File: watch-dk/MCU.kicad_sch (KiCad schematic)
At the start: 40 parts, among them IC301 FAN5624UMPX, IC302 MX25U51245GZ4I00, IC303 USBLC6-2P6, IC304 NTS0104GU12, J301 Jumper, J302 Jumper, J303 Jumper, J304 Jumper, M301 NORA-B106, X301 Power, X302 Power, X303 Device, X304 GPIO, X305 UART, X306 IO Power, X307 Display, X308 Touch Power, X309 LED Power, X310 DEBUG

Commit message: Task: Issue #129
Signed-off-by: Daniel Kampert <DanielKampert@kampis-elektroecke.de>
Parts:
- X301, X302: value Power -> Current
- X306: value IO Power -> IO Current
- X308: value Touch Power -> Touch Current
- X309: value LED Power -> LED Current
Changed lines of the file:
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@@
 			)
 		)
-		(property "Value" "Power"
+		(property "Value" "Current"
 			(at 54.61 63.5 0)
 			(effects
@@
 			)
 		)
-		(property "Value" "Power"
+		(property "Value" "Current"
 			(at 261.62 186.69 0)
 			(effects
@@
 			)
 		)
-		(property "Value" "Touch Power"
+		(property "Value" "Touch Current"
 			(at 365.76 118.1099 0)
 			(effects
@@
 			)
 		)
-		(property "Value" "IO Power"
+		(property "Value" "IO Current"
 			(at 341.63 118.1099 0)
 			(effects
@@
 			)
 		)
-		(property "Value" "LED Power"
+		(property "Value" "LED Current"
 			(at 377.19 166.3699 90)
 			(effects

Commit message: Feature: Issue #131
- Fix wrong page numbers
- Update reference designators to match the page numbers

Signed-off-by: Daniel Kampert <DanielKampert@kampis-elektroecke.de>
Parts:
- added S601: RESET, Wuerth:WS-TASV-6x6, symbol Switch:SW_Push
- renumbered C301 to C601, C302 to C602, C303 to C603, C304 to C604, IC301 to IC601, IC303 to IC602, IC302 to IC603, IC304 to IC604, J301 to J601, J302 to J602, J303 to J603, J304 to J604, M301 to M601, R301 to R601, R303 to R602, R304 to R603, R305 to R604, R306 to R605, R307 to R606, R308 to R607, R309 to R608, R310 to R609, R311 to R610, R312 to R611, R302 to R612, R315 to R613, R316 to R614, R313 to R615, R314 to R616, TP301 to TP601, X310 to X601, X301 to X602, X303 to X603, X305 to X604, X304 to X605, X302 to X606, X306 to X607, X307 to X608, X308 to X609, X309 to X610
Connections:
- net GND: now also S601.2
- net RESETn: now also S601.1
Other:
- moved on the sheet: C602, IC603, J601, R612, X606

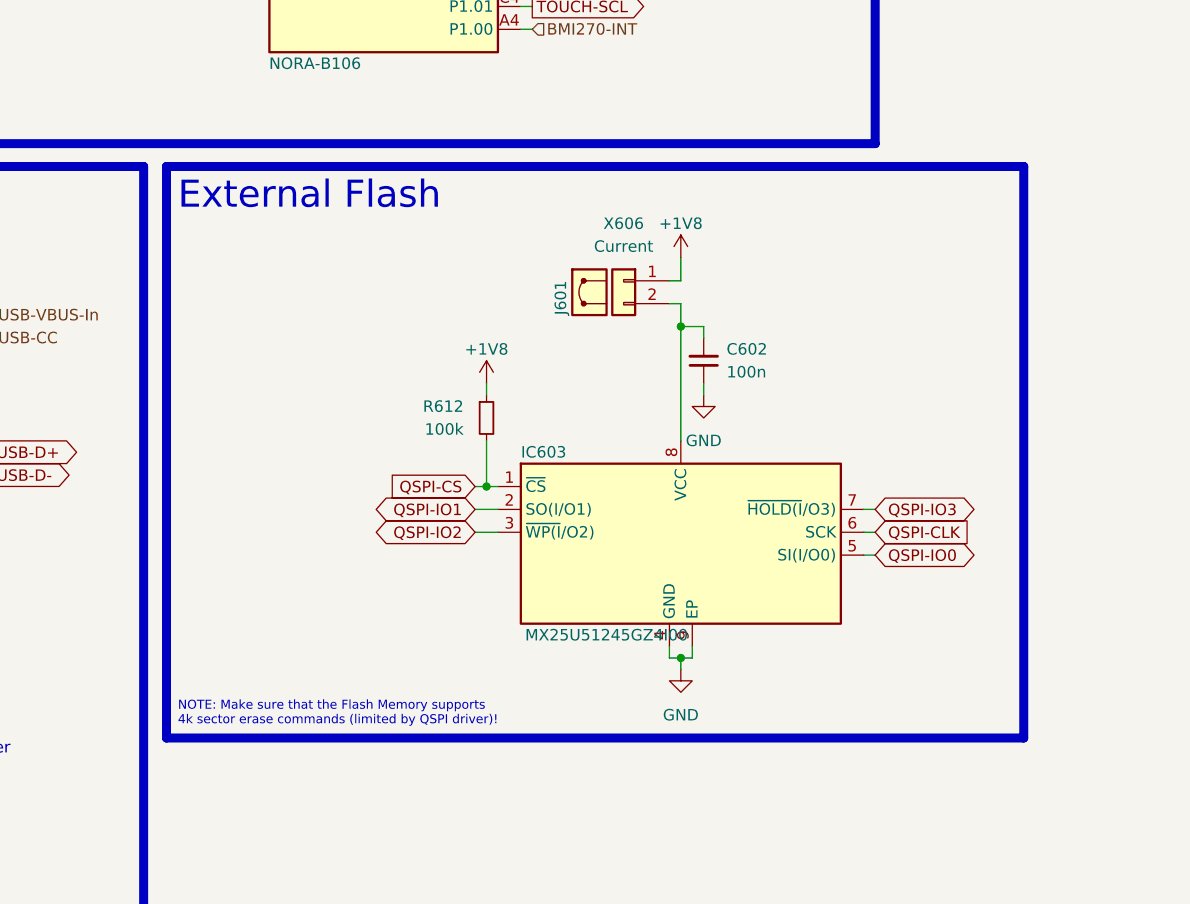
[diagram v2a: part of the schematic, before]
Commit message: Bug: Issue #132
Signed-off-by: Daniel Kampert <DanielKampert@kampis-elektroecke.de>
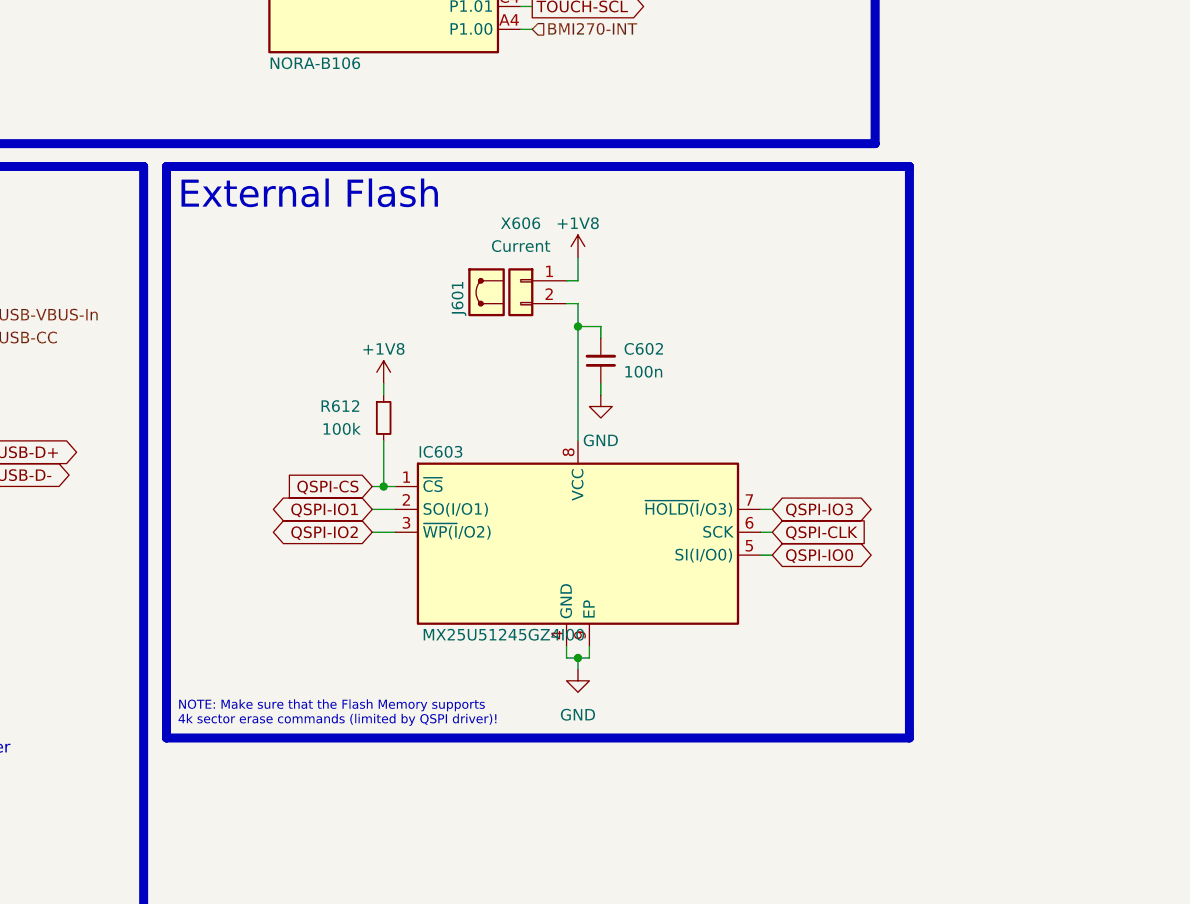
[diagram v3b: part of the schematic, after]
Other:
- moved on the sheet: C602, IC603, J601, R612, X606

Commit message: Feature: Issue #133
Signed-off-by: Daniel Kampert <DanielKampert@kampis-elektroecke.de>
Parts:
- IC604: symbol NXP:NTS0104GU12 -> NXP:NTS0104GU12 (XQFN12)
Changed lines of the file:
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@@
 	)
 	(symbol
-		(lib_id "NXP:NTS0104GU12")
+		(lib_id "NXP:NTS0104GU12 (XQFN12)")
 		(at 351.79 76.2 0)
 		(unit 1)
@@
 		)
 		(property "Footprint" "Package_QFN:XQFN-12-1.7x2mm_P0.4mm"
-			(at 353.06 73.66 0)
+			(at 351.79 76.2 0)
 			(effects
 				(font
@@
 		)
 		(property "Datasheet" "https://www.nxp.com/docs/en/data-sheet/NTS0104.pdf"
-			(at 353.06 73.66 0)
+			(at 351.79 76.2 0)
 			(effects
 				(font

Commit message: Bug: Issue #134
Signed-off-by: Daniel Kampert <DanielKampert@kampis-elektroecke.de>
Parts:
- C601: manf# 04023D105KAT2A -> 0402YC105JAT2A; mouser# 581-04023D105KAT2A -> 581-0402YC105JAT2A
- IC601: value FAN5624UMPX -> FAN5622SX; footprint Package_DFN_QFN:UQFN-10_1.4x1.8mm_P0.4mm -> Package_TO_SOT_SMD:TSOT-23-6; symbol ON Semiconductor:FAN5624 -> ON Semiconductor:FAN5622SX; manf# FAN5624UMPX -> FAN5622SX; mouser# 512-FAN5624UMPX -> 512-FAN5622SX
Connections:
- net DISPLAY-BLK: now also IC601.1 (CTRL); no longer IC601.7 (CTRL)
- net GND: now also IC601.2 (GND), R601.1; no longer IC601.6 (GND), R601.2
- net LEDK1: now also IC601.6 (LED1); no longer IC601.8 (LED1)
- net LEDK2: now also IC601.4 (LED2); no longer IC601.10 (LED2)
- net at IC601.3 (VIN): now also C601.2, R602.2; no longer R601.1
- new net: IC601.5 (ISET), R601.2
- no-connect marks 13 -> 11
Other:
- moved on the sheet: C601, J602, J604, R601

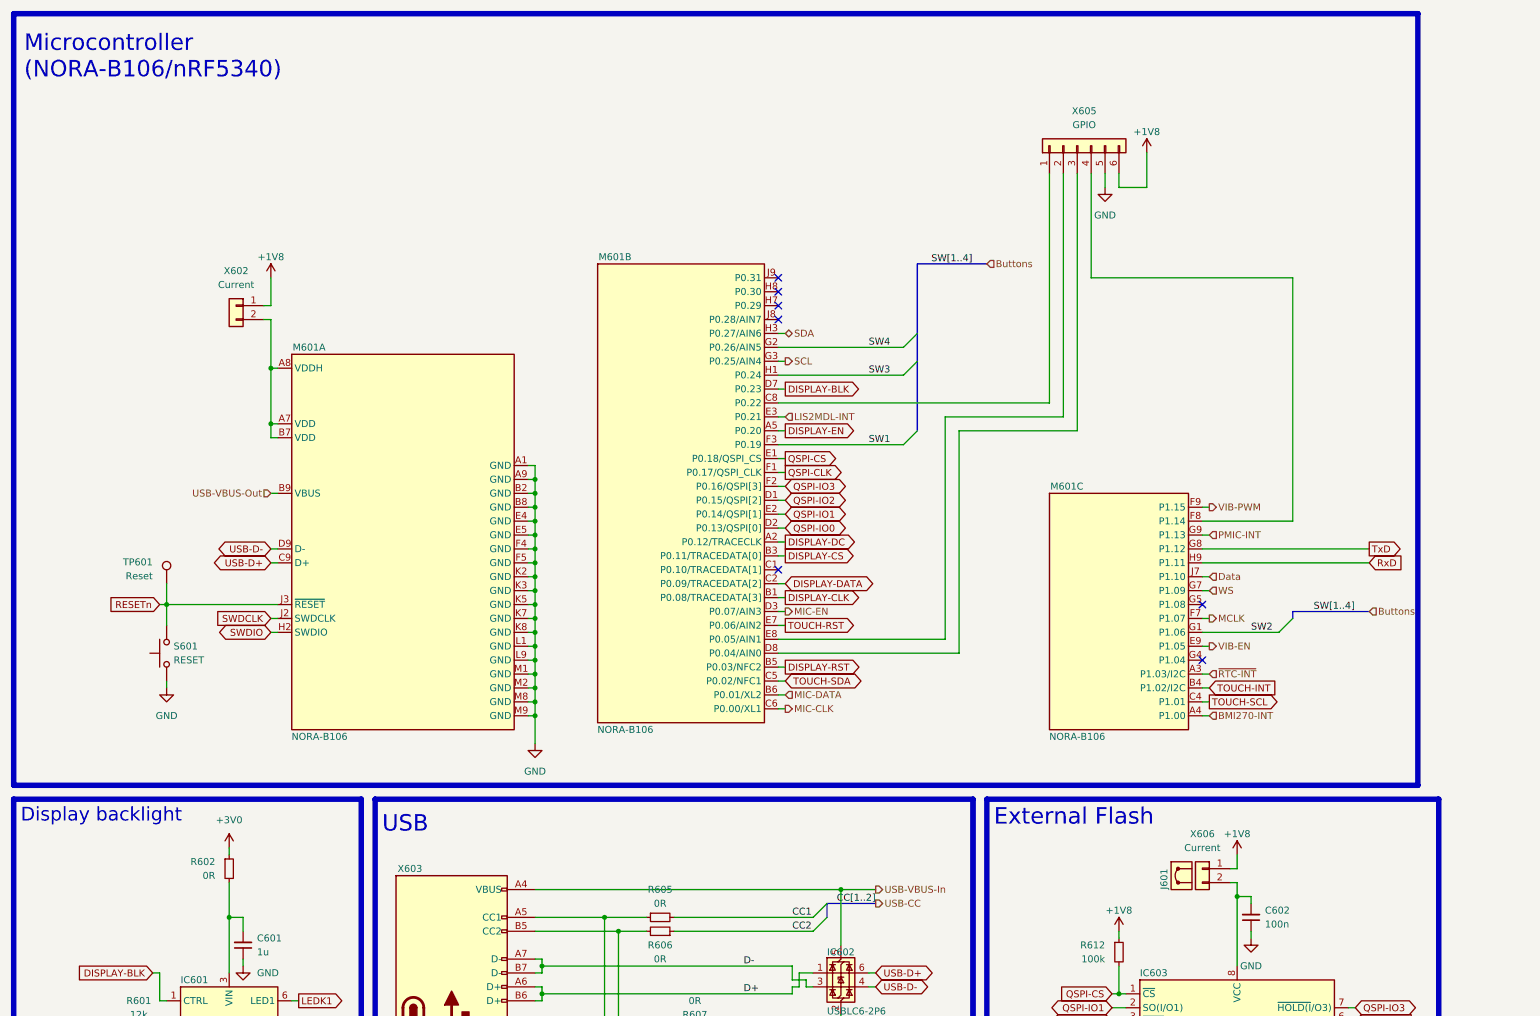
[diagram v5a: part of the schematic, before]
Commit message: doc: CI/CD fixes, documentation updates
- Fix wrong part number for SWD connector
- Fix missing footprint for RTC level shifter

Signed-off-by: Daniel Kampert <DanielKampert@kampis-elektroecke.de>
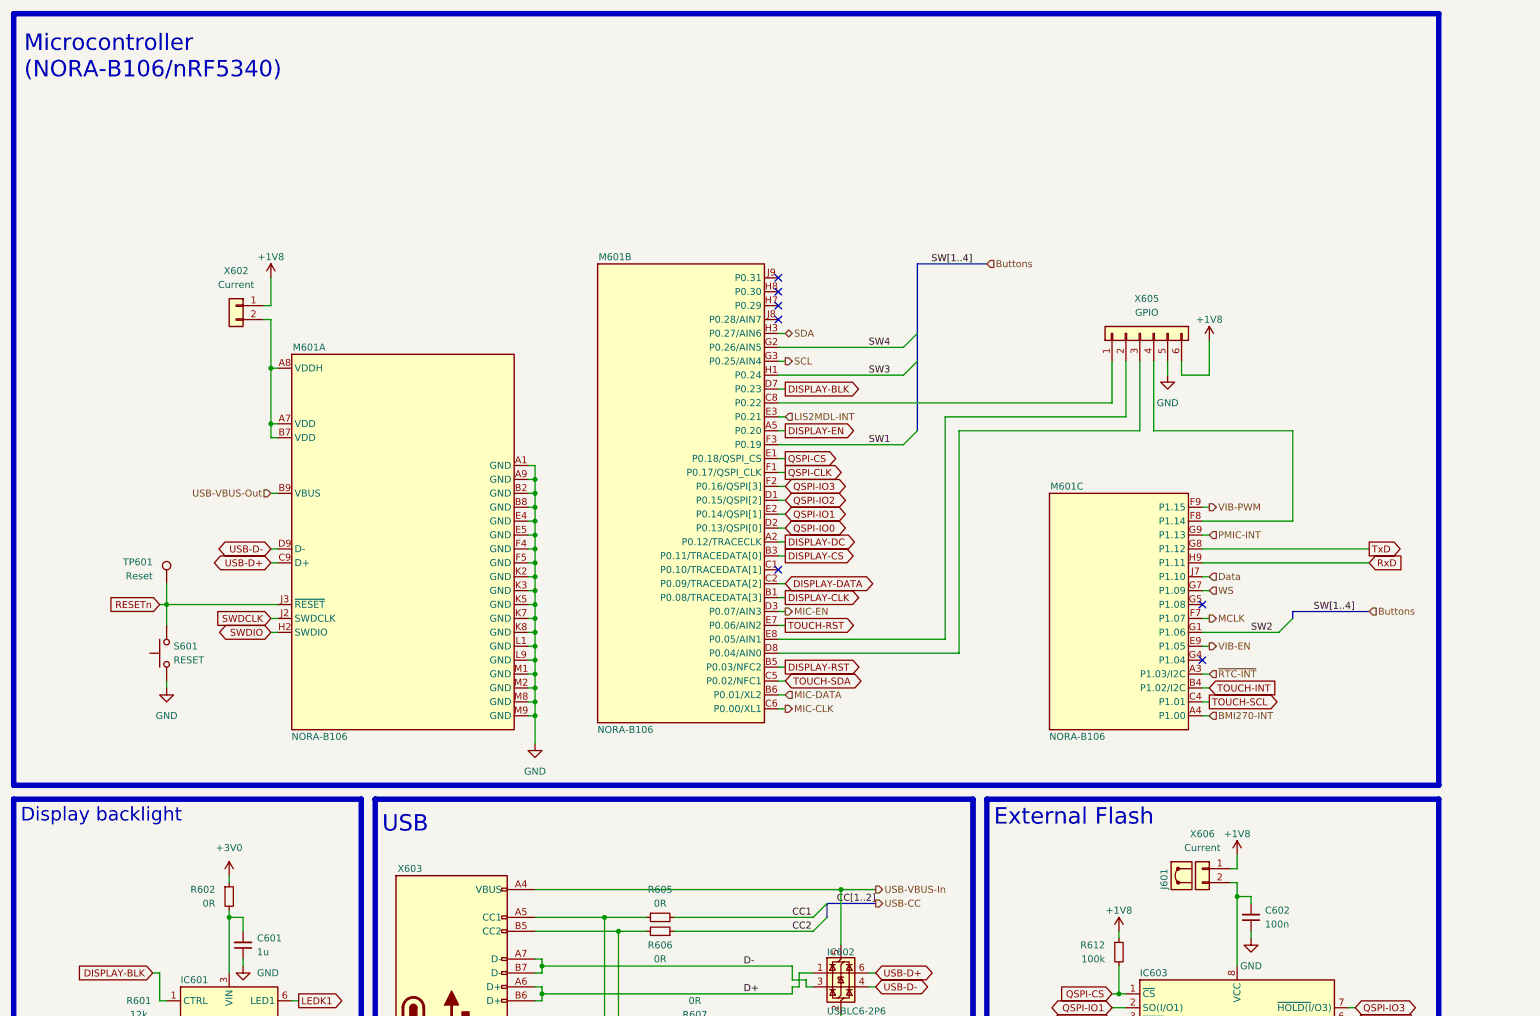
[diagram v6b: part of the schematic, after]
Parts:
- X601: manf# 623310235521 -> 62101021021; mouser# 710-623310235521 -> 710-62101021021
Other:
- moved on the sheet: R602, X605
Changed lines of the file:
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@@
 	(polyline
 		(pts
-			(xy 270.51 13.97) (xy 13.97 13.97)
+			(xy 274.32 13.97) (xy 13.97 13.97)
 		)
 		(stroke
@@
 	(polyline
 		(pts
-			(xy 270.51 154.94) (xy 13.97 154.94)
+			(xy 274.32 154.94) (xy 13.97 154.94)
 		)
 		(stroke
@@
 	(wire
 		(pts
-			(xy 53.34 166.37) (xy 53.34 167.64)
+			(xy 53.34 171.45) (xy 53.34 172.72)
 		)
 		(stroke
@@
 	(wire
 		(pts
-			(xy 247.65 106.68) (xy 247.65 62.23)
+			(xy 247.65 106.68) (xy 247.65 90.17)
 		)
 		(stroke
@@
 	(wire
 		(pts
-			(xy 203.2 43.18) (xy 203.2 85.09)
+			(xy 214.63 77.47) (xy 214.63 85.09)
 		)
 		(stroke
@@
 	(wire
 		(pts
-			(xy 220.98 39.37) (xy 220.98 45.72)
+			(xy 232.41 73.66) (xy 232.41 80.01)
 		)
 		(stroke
@@
 	(wire
 		(pts
-			(xy 205.74 43.18) (xy 205.74 87.63)
+			(xy 217.17 77.47) (xy 217.17 87.63)
 		)
 		(stroke
@@
 	(wire
 		(pts
-			(xy 205.74 87.63) (xy 184.15 87.63)
+			(xy 217.17 87.63) (xy 184.15 87.63)
 		)
 		(stroke
@@
 	(wire
 		(pts
-			(xy 208.28 90.17) (xy 186.69 90.17)
+			(xy 219.71 90.17) (xy 186.69 90.17)
 		)
 		(stroke
@@
 	(polyline
 		(pts
-			(xy 270.51 13.97) (xy 270.51 154.94)
+			(xy 274.32 13.97) (xy 274.32 154.94)
 		)
 		(stroke
@@
 	(wire
 		(pts
-			(xy 208.28 43.18) (xy 208.28 90.17)
+			(xy 219.71 77.47) (xy 219.71 90.17)
 		)
 		(stroke
@@
 	(wire
 		(pts
-			(xy 213.36 43.18) (xy 213.36 45.72)
+			(xy 224.79 77.47) (xy 224.79 80.01)
 		)
 		(stroke
@@
 	(wire
 		(pts
-			(xy 247.65 62.23) (xy 210.82 62.23)
+			(xy 247.65 90.17) (xy 222.25 90.17)
 		)
 		(stroke
@@
 	(wire
 		(pts
-			(xy 215.9 45.72) (xy 215.9 43.18)
+			(xy 227.33 80.01) (xy 227.33 77.47)
 		)
 		(stroke
@@
 	(wire
 		(pts
-			(xy 220.98 45.72) (xy 215.9 45.72)
+			(xy 232.41 80.01) (xy 227.33 80.01)
 		)
 		(stroke
@@
 	(wire
 		(pts
-			(xy 153.67 85.09) (xy 203.2 85.09)
+			(xy 153.67 85.09) (xy 214.63 85.09)
 		)
 		(stroke
@@
 	(wire
 		(pts
-			(xy 210.82 43.18) (xy 210.82 62.23)
+			(xy 222.25 77.47) (xy 222.25 90.17)
 		)
 		(stroke
@@
 	(wire
 		(pts
-			(xy 53.34 172.72) (xy 53.34 179.07)
+			(xy 53.34 177.8) (xy 53.34 179.07)
 		)
 		(stroke
@@
 			)
 		)
-		(property "manf#" "623310235521"
+		(property "manf#" "62101021021"
 			(at 41.91 255.27 0)
 			(effects
@@
 			)
 		)
-		(property "mouser#" "710-623310235521"
+		(property "mouser#" "710-62101021021"
 			(at 41.91 255.27 0)
 			(effects
@@
 	(symbol
 		(lib_id "power:+1V8")
-		(at 220.98 39.37 0)
+		(at 232.41 73.66 0)
 		(unit 1)
 		(exclude_from_sim no)
@@
 		(fields_autoplaced yes)
 		(property "Reference" "#PWR0617"
-			(at 220.98 43.18 0)
+			(at 232.41 77.47 0)
 			(effects
 				(font
@@
 		)
 		(property "Value" "+1V8"
-			(at 220.98 35.56 0)
+			(at 232.41 69.85 0)
 			(effects
 				(font
@@
 		)
 		(property "Footprint" ""
-			(at 220.98 39.37 0)
+			(at 232.41 73.66 0)
 			(effects
 				(font
@@
 		)
 		(property "Datasheet" ""
-			(at 220.98 39.37 0)
+			(at 232.41 73.66 0)
 			(effects
 				(font
@@
 		)
 		(property "Description" ""
-			(at 220.98 39.37 0)
+			(at 232.41 73.66 0)
 			(effects
 				(font
@@
 	(symbol
 		(lib_id "power:+3V0")
-		(at 53.34 166.37 0)
+		(at 53.34 171.45 0)
 		(unit 1)
 		(exclude_from_sim no)
@@
 		(fields_autoplaced yes)
 		(property "Reference" "#PWR0605"
-			(at 53.34 170.18 0)
+			(at 53.34 175.26 0)
 			(effects
 				(font
@@
 		)
 		(property "Value" "+3V0"
-			(at 53.34 161.29 0)
+			(at 53.34 166.37 0)
 			(effects
 				(font
@@
 		)
 		(property "Footprint" ""
-			(at 53.34 166.37 0)
+			(at 53.34 171.45 0)
 			(effects
 				(font
@@
 		)
 		(property "Datasheet" ""
-			(at 53.34 166.37 0)
+			(at 53.34 171.45 0)
 			(effects
 				(font
@@
 		)
 		(property "Description" "Power symbol creates a global label with name \"+3V0\""
-			(at 53.34 166.37 0)
+			(at 53.34 171.45 0)
 			(effects
 				(font
@@
 		)
 		(property "manf" ""
-			(at 53.34 166.37 0)
+			(at 53.34 171.45 0)
 			(effects
 				(font
@@
 		)
 		(property "manf#" ""
-			(at 53.34 166.37 0)
+			(at 53.34 171.45 0)
 			(effects
 				(font
@@
 		)
 		(property "Distributor" ""
-			(at 53.34 166.37 0)
+			(at 53.34 171.45 0)
 			(effects
 				(font
@@
 		)
 		(property "mouser#" ""
-			(at 53.34 166.37 0)
+			(at 53.34 171.45 0)
 			(effects
 				(font
@@
 		)
 		(property "CONFIG" ""
-			(at 53.34 166.37 0)
+			(at 53.34 171.45 0)
 			(effects
 				(font
@@
 	(symbol
 		(lib_id "Connector_Generic:Conn_01x06")
-		(at 208.28 38.1 90)
+		(at 219.71 72.39 90)
 		(unit 1)
 		(exclude_from_sim no)
@@
 		(fields_autoplaced yes)
 		(property "Reference" "X605"
-			(at 209.55 31.75 90)
+			(at 220.98 66.04 90)
 			(effects
 				(font
@@
 		)
 		(property "Value" "GPIO"
-			(at 209.55 34.29 90)
+			(at 220.98 68.58 90)
 			(effects
 				(font
@@
 		)
 		(property "Footprint" "Connector_PinHeader_2.54mm:PinHeader_1x06_P2.54mm_Vertical"
-			(at 208.28 38.1 0)
+			(at 219.71 72.39 0)
 			(effects
 				(font
@@
 		)
 		(property "Datasheet" "https://cdn.amphenol-cs.com/media/wysiwyg/files/documentation/datasheet/boardwiretoboard/bwb_econostik_254headers.pdf"
-			(at 208.28 38.1 0)
+			(at 219.71 72.39 0)
 			(effects
 				(font
@@
 		)
 		(property "Description" "Generic connector, single row, 01x06, script generated (kicad-library-utils/schlib/autogen/connector/)"
-			(at 208.28 38.1 0)
+			(at 219.71 72.39 0)
 			(effects
 				(font
@@
 		)
 		(property "manf" "Amphenol FCI"
-			(at 208.28 38.1 0)
+			(at 219.71 72.39 0)
 			(effects
 				(font
@@
 		)
 		(property "manf#" "77311-802-06LF"
-			(at 208.28 38.1 0)
+			(at 219.71 72.39 0)
 			(effects
 				(font
@@
 		)
 		(property "mouser#" "649-77311-802-06LF"
-			(at 208.28 38.1 0)
+			(at 219.71 72.39 0)
 			(effects
 				(font
@@
 		)
 		(property "CONFIG" ""
-			(at 208.28 38.1 0)
+			(at 219.71 72.39 0)
 			(effects
 				(font
@@
 	(symbol
 		(lib_id "Device:R_Small")
-		(at 53.34 170.18 0)
+		(at 53.34 175.26 0)
 		(unit 1)
 		(exclude_from_sim no)
@@
 		(dnp no)
 		(property "Reference" "R602"
-			(at 50.8 168.91 0)
+			(at 50.8 173.99 0)
 			(effects
 				(font
@@
 		)
 		(property "Value" "0R"
-			(at 50.8 171.45 0)
+			(at 50.8 176.53 0)
 			(effects
 				(font
@@
 		)
 		(property "Footprint" "Resistor_SMD:R_0805_2012Metric"
-			(at 53.34 170.18 0)
+			(at 53.34 175.26 0)
 			(effects
 				(font
@@
 		)
 		(property "Datasheet" "https://www.mouser.de/datasheet/2/54/cr-1858361.pdf"
-			(at 53.34 170.18 0)
+			(at 53.34 175.26 0)
 			(effects
 				(font
@@
 		)
 		(property "Description" ""
-			(at 53.34 170.18 0)
+			(at 53.34 175.26 0)
 			(effects
 				(font
@@
 		)
 		(property "CONFIG" ""
-			(at 53.34 170.18 0)
+			(at 53.34 175.26 0)
 			(effects
 				(font
@@
 		)
 		(property "manf" "Bourns"
-			(at 53.34 170.18 0)
+			(at 53.34 175.26 0)
 			(effects
 				(font
@@
 		)
 		(property "manf#" "CR0805-J/-000ELF"
-			(at 53.34 170.18 0)
+			(at 53.34 175.26 0)
 			(effects
 				(font
@@
 		)
 		(property "mouser#" "652-CR0805-J/-000ELF"
-			(at 53.34 170.18 0)
+			(at 53.34 175.26 0)
 			(effects
 				(font
@@
 	(symbol
 		(lib_id "power:GND")
-		(at 213.36 45.72 0)
+		(at 224.79 80.01 0)
 		(unit 1)
 		(exclude_from_sim no)
@@
 		(dnp no)
 		(property "Reference" "#PWR0615"
-			(at 213.36 52.07 0)
+			(at 224.79 86.36 0)
 			(effects
 				(font
@@
 		)
 		(property "Value" "GND"
-			(at 213.36 50.8 0)
+			(at 224.79 85.09 0)
 			(effects
 				(font
@@
 		)
 		(property "Footprint" ""
-			(at 213.36 45.72 0)
+			(at 224.79 80.01 0)
 			(effects
 				(font
@@
 		)
 		(property "Datasheet" ""
-			(at 213.36 45.72 0)
+			(at 224.79 80.01 0)
 			(effects
 				(font
@@
 		)
 		(property "Description" ""
-			(at 213.36 45.72 0)
+			(at 224.79 80.01 0)
 			(effects
 				(font
